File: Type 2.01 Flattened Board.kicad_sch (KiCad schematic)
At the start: 8 parts, among them U10 74AHC125

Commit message: Do the majority of the routing
Drop the i960 header breakout, also don't connect LOCK to the management
engine. I have no idea what it would be useful for. The chipset is the
only thing that will directly interact with the i960 so locking isn't
necessary.
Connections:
- net BUS.PB18: now also U10.10
- net BUS.PB2: now also U10.4
- net BUS.PB4: now also XA2.A3
- net BUS.PB5: now also XA2.A4
- net BUS.PB6: now also XA2.A5
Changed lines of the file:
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@@
-    (stroke (width 0) (type default) (color 0 0 0 0))
-  )
-  (bus_entry (at 246.38 86.36) (size 2.54 2.54)
     (stroke (width 0) (type default) (color 0 0 0 0))
   )
@@
     (stroke (width 0) (type default) (color 0 0 0 0))
   )
-  (bus_entry (at 236.22 86.36) (size 2.54 2.54)
+  (bus_entry (at 241.3 86.36) (size 2.54 2.54)
     (stroke (width 0) (type default) (color 0 0 0 0))
   )
@@
     (stroke (width 0) (type default) (color 0 0 0 0))
   )
-  (bus_entry (at 241.3 86.36) (size 2.54 2.54)
-    (stroke (width 0) (type default) (color 0 0 0 0))
-  )
-  (bus_entry (at 243.84 86.36) (size 2.54 2.54)
-    (stroke (width 0) (type default) (color 0 0 0 0))
-  )
   (bus_entry (at 309.499 142.24) (size 2.54 2.54)
     (stroke (width 0) (type default) (color 0 0 0 0))
@@
     (stroke (width 0) (type default) (color 0 0 0 0))
   )
-  (bus_entry (at 233.68 86.36) (size 2.54 2.54)
-    (stroke (width 0) (type default) (color 0 0 0 0))
-  )
   (bus_entry (at 187.452 106.172) (size 2.54 2.54)
     (stroke (width 0) (type default) (color 0 0 0 0))
@@
     (stroke (width 0) (type default) (color 0 0 0 0))
   )
-  (wire (pts (xy 236.22 88.9) (xy 236.22 102.87))
-    (stroke (width 0) (type default) (color 0 0 0 0))
-  )
   (wire (pts (xy 77.343 253.365) (xy 46.863 253.365))
     (stroke (width 0) (type default) (color 0 0 0 0))
@@
     (stroke (width 0) (type default) (color 0 0 0 0))
   )
-  (wire (pts (xy 238.76 88.9) (xy 238.76 102.87))
-    (stroke (width 0) (type default) (color 0 0 0 0))
-  )
   (wire (pts (xy 139.7 172.212) (xy 187.452 172.212))
     (stroke (width 0) (type default) (color 0 0 0 0))
@@
   )
   (bus (pts (xy 309.499 106.68) (xy 309.499 109.22))
-    (stroke (width 0) (type default) (color 0 0 0 0))
-  )
-  (wire (pts (xy 248.92 88.9) (xy 248.92 102.87))
-    (stroke (width 0) (type default) (color 0 0 0 0))
-  )
-  (wire (pts (xy 246.38 88.9) (xy 246.38 102.87))
     (stroke (width 0) (type default) (color 0 0 0 0))
   )
@@
     (effects (font (size 1.27 1.27)) (justify left bottom))
   )
-  (label "BUS.PB4" (at 28.575 203.2 180)
-    (effects (font (size 1.27 1.27)) (justify right bottom))
+  (label "BUS.PB4" (at 33.655 235.585 0)
+    (effects (font (size 1.27 1.27)) (justify left bottom))
   )
   (label "BUS.PC15" (at 145.288 154.432 0)
@@
     (effects (font (size 1.27 1.27)) (justify right bottom))
   )
+  (label "BUS.PB18" (at 289.56 248.285 180)
+    (effects (font (size 1.27 1.27)) (justify right bottom))
+  )
   (label "BUS.PB12" (at 59.182 80.772 0)
     (effects (font (size 1.27 1.27)) (justify left bottom))
   )
-  (label "BUS.PB1" (at 348.615 95.25 180)
+  (label "BUS.PB1" (at 241.3 89.535 270)
     (effects (font (size 1.27 1.27)) (justify right bottom))
   )
@@
     (effects (font (size 1.27 1.27)) (justify left bottom))
   )
-  (label "BUS.PB6" (at 384.81 86.36 180)
-    (effects (font (size 1.27 1.27)) (justify right bottom))
+  (label "BUS.PB6" (at 33.655 230.505 0)
+    (effects (font (size 1.27 1.27)) (justify left bottom))
   )
   (label "SPI_MOSI" (at 102.87 42.164 270)
@@
     (effects (font (size 1.27 1.27)) (justify left bottom))
   )
-  (label "BUS.PB7" (at 383.54 67.945 180)
+  (label "BUS.PB7" (at 243.84 89.535 270)
     (effects (font (size 1.27 1.27)) (justify right bottom))
   )
@@
     (effects (font (size 1.27 1.27)) (justify right bottom))
   )
-  (label "BUS.PB5" (at 28.575 205.74 180)
-    (effects (font (size 1.27 1.27)) (justify right bottom))
+  (label "BUS.PB5" (at 33.655 233.045 0)
+    (effects (font (size 1.27 1.27)) (justify left bottom))
   )
   (label "GCM4.D7" (at 312.547 124.46 0)
@@
   (label "BUS.PA15" (at 145.288 106.172 0)
     (effects (font (size 1.27 1.27)) (justify left bottom))
+  )
+  (label "BUS.PB2" (at 289.56 228.6 180)
+    (effects (font (size 1.27 1.27)) (justify right bottom))
   )
   (label "BUS.PA17" (at 145.288 139.192 0)
@@
       (reference "C37") (unit 1) (value "0.1uF") (footprint "Capacitor_SMD:C_0805_2012Metric_Pad1.18x1.45mm_HandSolder")
     )
-    (path "/cd4173d7-5549-43d9-b4b1-83989500a84c/15588c18-b55b-4c7c-83c0-ba9a59dc7e6e"
-      (reference "J3") (unit 1) (value "Conn_01x05") (footprint "Connector_PinHeader_2.54mm:PinHeader_1x05_P2.54mm_Vertical")
-    )
     (path "/cd4173d7-5549-43d9-b4b1-83989500a84c/32cf6c22-092f-47a1-90de-a0ed44f63e14"
       (reference "J5") (unit 1) (value "Conn_02x03_Odd_Even") (footprint "Connector_IDC:IDC-Header_2x03_P2.54mm_Horizontal")
@@
       (reference "R3") (unit 1) (value "10k") (footprint "Resistor_SMD:R_0805_2012Metric_Pad1.20x1.40mm_HandSolder")
     )
-    (path "/cd4173d7-5549-43d9-b4b1-83989500a84c/d8f2a0bf-f685-461e-9c59-599184f44107"
-      (reference "R5") (unit 1) (value "10k") (footprint "Resistor_SMD:R_0805_2012Metric_Pad1.20x1.40mm_HandSolder")
-    )
     (path "/cd4173d7-5549-43d9-b4b1-83989500a84c/300496ea-2d26-4906-8c04-178876ec4114"

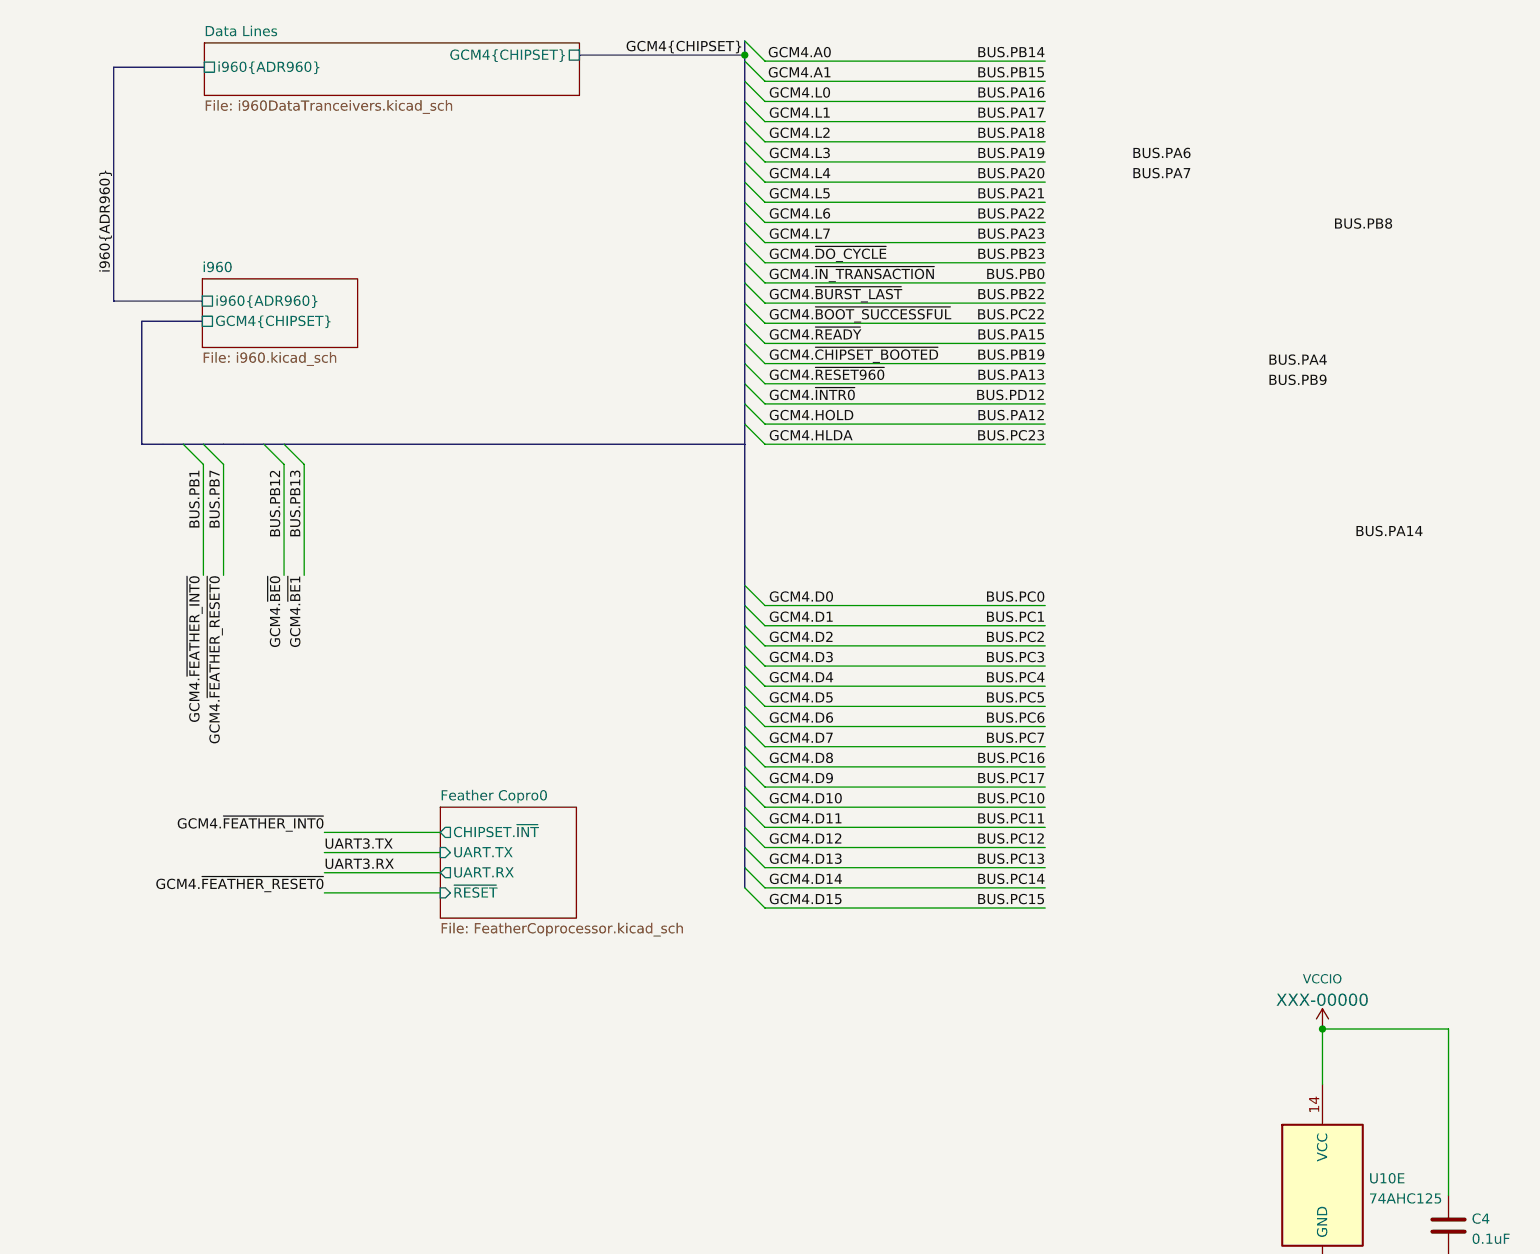
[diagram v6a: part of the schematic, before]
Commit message: Have enough free pins with a serial connection for a second feather coprocessor socket
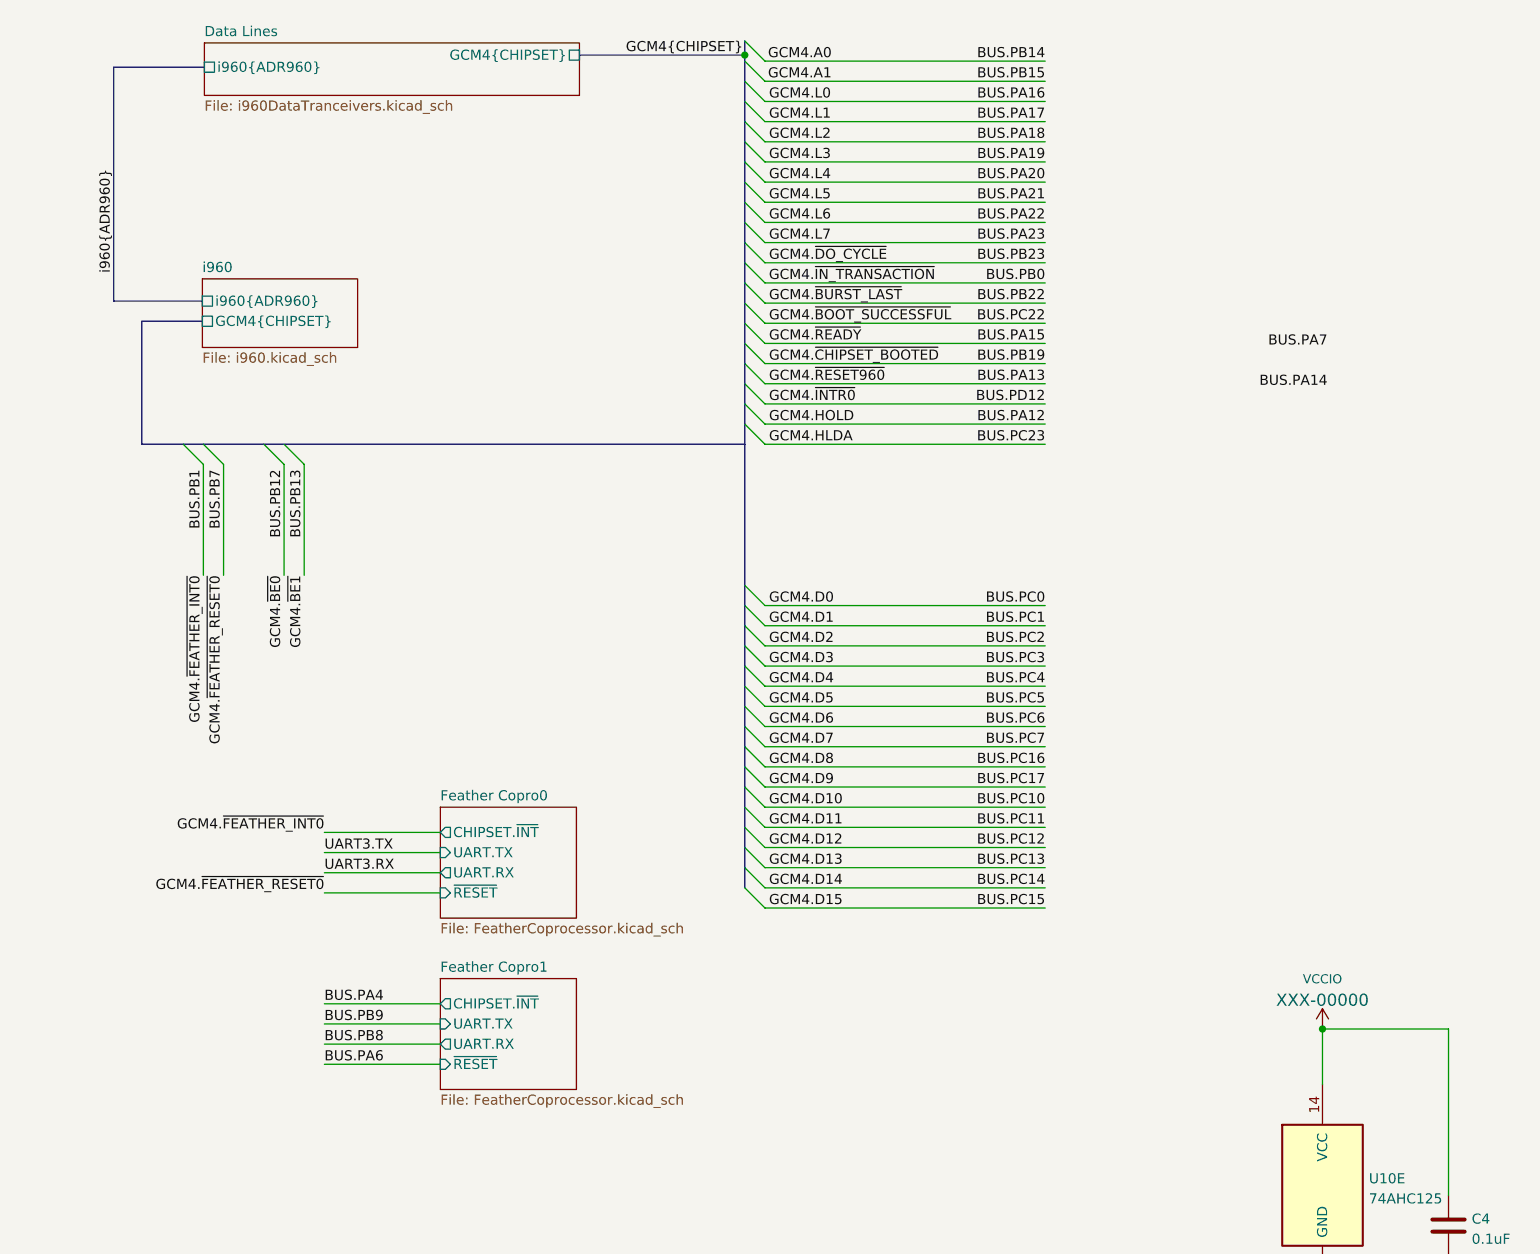
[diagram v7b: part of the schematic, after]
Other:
- added sheet Feather Copro1 (FeatherCoprocessor.kicad_sch)
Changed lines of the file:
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@@
+    (stroke (width 0) (type default) (color 0 0 0 0))
+  )
+  (wire (pts (xy 256.54 164.465) (xy 271.145 164.465))
     (stroke (width 0) (type default) (color 0 0 0 0))
   )
@@
     (stroke (width 0) (type default) (color 0 0 0 0))
   )
+  (wire (pts (xy 256.54 156.845) (xy 271.145 156.845))
+    (stroke (width 0) (type default) (color 0 0 0 0))
+  )
   (bus (pts (xy 309.499 139.7) (xy 309.499 142.24))
     (stroke (width 0) (type default) (color 0 0 0 0))
@@
     (stroke (width 0) (type default) (color 0 0 0 0))
   )
-  (bus (pts (xy 246.38 86.36) (xy 248.92 86.36))
+  (bus (pts (xy 241.3 86.36) (xy 248.92 86.36))
     (stroke (width 0) (type default) (color 0 0 0 0))
   )
@@
     (stroke (width 0) (type default) (color 0 0 0 0))
   )
+  (wire (pts (xy 256.54 159.385) (xy 271.145 159.385))
+    (stroke (width 0) (type default) (color 0 0 0 0))
+  )
   (wire (pts (xy 312.039 116.84) (xy 347.345 116.84))
     (stroke (width 0) (type default) (color 0 0 0 0))
@@
     (stroke (width 0) (type default) (color 0 0 0 0))
   )
-  (bus (pts (xy 233.68 86.36) (xy 236.22 86.36))
+  (bus (pts (xy 233.68 86.36) (xy 238.76 86.36))
     (stroke (width 0) (type default) (color 0 0 0 0))
   )
@@
     (stroke (width 0) (type default) (color 0 0 0 0))
   )
-  (bus (pts (xy 241.3 86.36) (xy 243.84 86.36))
-    (stroke (width 0) (type default) (color 0 0 0 0))
-  )
   (wire (pts (xy 25.908 73.152) (xy 73.66 73.152))
     (stroke (width 0) (type default) (color 0 0 0 0))
@@
     (stroke (width 0) (type default) (color 0 0 0 0))
   )
-  (bus (pts (xy 236.22 86.36) (xy 238.76 86.36))
-    (stroke (width 0) (type default) (color 0 0 0 0))
-  )
   (bus (pts (xy 309.499 106.68) (xy 309.499 109.22))
     (stroke (width 0) (type default) (color 0 0 0 0))
@@
     (stroke (width 0) (type default) (color 0 0 0 0))
   )
+  (wire (pts (xy 256.54 161.925) (xy 271.145 161.925))
+    (stroke (width 0) (type default) (color 0 0 0 0))
+  )
   (bus (pts (xy 23.368 118.872) (xy 23.368 116.332))
     (stroke (width 0) (type default) (color 0 0 0 0))
@@
   )
   (wire (pts (xy 139.7 96.012) (xy 187.452 96.012))
-    (stroke (width 0) (type default) (color 0 0 0 0))
-  )
-  (bus (pts (xy 243.84 86.36) (xy 246.38 86.36))
     (stroke (width 0) (type default) (color 0 0 0 0))
   )
@@
     (effects (font (size 1.27 1.27)) (justify left bottom))
   )
-  (label "BUS.PB8" (at 391.16 59.69 180)
-    (effects (font (size 1.27 1.27)) (justify right bottom))
+  (label "BUS.PB8" (at 256.54 161.925 0)
+    (effects (font (size 1.27 1.27)) (justify left bottom))
   )
   (label "BUS.PB6" (at 61.214 129.032 0)
@@
     (effects (font (size 1.27 1.27)) (justify left bottom))
   )
-  (label "BUS.PA4" (at 382.905 76.835 180)
-    (effects (font (size 1.27 1.27)) (justify right bottom))
+  (label "BUS.PA4" (at 256.54 156.845 0)
+    (effects (font (size 1.27 1.27)) (justify left bottom))
   )
   (label "BUS.PD12" (at 145.288 103.632 0)
@@
     (effects (font (size 1.27 1.27)) (justify left bottom))
   )
-  (label "BUS.PA14" (at 394.97 98.425 180)
+  (label "BUS.PA14" (at 382.905 79.375 180)
     (effects (font (size 1.27 1.27)) (justify right bottom))
   )
@@
     (effects (font (size 1.27 1.27)) (justify right bottom))
   )
-  (label "BUS.PA6" (at 365.76 50.8 180)
-    (effects (font (size 1.27 1.27)) (justify right bottom))
+  (label "BUS.PA6" (at 256.54 164.465 0)
+    (effects (font (size 1.27 1.27)) (justify left bottom))
   )
   (label "BUS.PC1" (at 61.214 116.332 0)
@@
     (effects (font (size 1.27 1.27)) (justify left bottom))
   )
-  (label "BUS.PA7" (at 365.76 53.34 180)
+  (label "BUS.PA7" (at 382.905 74.295 180)
     (effects (font (size 1.27 1.27)) (justify right bottom))
   )
@@
     (effects (font (size 1.27 1.27)) (justify left bottom))
   )
-  (label "BUS.PB9" (at 382.905 79.375 180)
-    (effects (font (size 1.27 1.27)) (justify right bottom))
+  (label "BUS.PB9" (at 256.54 159.385 0)
+    (effects (font (size 1.27 1.27)) (justify left bottom))
   )
   (label "BUS.PB14" (at 347.345 38.1 180)
@@
     (pin "7")
   )
+  (sheet (at 271.145 153.67) (size 17.145 13.97) (fields_autoplaced)
+    (stroke (width 0.1524) (type solid) (color 0 0 0 0))
+    (fill (color 0 0 0 0.0000))
+    (property "Sheet name" "Feather Copro1" (id 0) (at 271.145 152.9584 0)
+      (effects (font (size 1.27 1.27)) (justify left bottom))
+    )
+    (property "Sheet file" "FeatherCoprocessor.kicad_sch" (id 1) (at 271.145 168.2246 0)
+      (effects (font (size 1.27 1.27)) (justify left top))
+    )
+    (pin "CHIPSET.~{INT}" output (at 271.145 156.845 180)
+      (effects (font (size 1.27 1.27)) (justify left))
+    )
+    (pin "UART.TX" input (at 271.145 159.385 180)
+      (effects (font (size 1.27 1.27)) (justify left))
+    )
+    (pin "UART.RX" output (at 271.145 161.925 180)
+      (effects (font (size 1.27 1.27)) (justify left))
+    )
+    (pin "~{RESET}" input (at 271.145 164.465 180)
+      (effects (font (size 1.27 1.27)) (justify left))
+    )
+  )
   (sheet (at 241.427 35.814) (size 47.244 6.604) (fields_autoplaced)
     (stroke (width 0.1524) (type solid) (color 0 0 0 0))
@@
   (sheet_instances
     (path "/" (page "1"))
+    (path "/33147676-43f8-493a-9a6a-8cf437a2c6b4" (page "2"))
     (path "/cd4173d7-5549-43d9-b4b1-83989500a84c/099401c1-0181-4257-be0f-4c7f9d47aefb" (page "3"))
     (path "/c9365d17-b900-4bd3-b96d-5359e9255bd9" (page "7"))
@@
       (reference "#FLG0102") (unit 1) (value "PWR_FLAG") (footprint "")
     )
+    (path "/33147676-43f8-493a-9a6a-8cf437a2c6b4/b66c4163-6664-4006-bf2a-84dc4b6cdd35"
+      (reference "#PWR01") (unit 1) (value "+3.3V") (footprint "")
+    )
+    (path "/33147676-43f8-493a-9a6a-8cf437a2c6b4/83c89139-f22f-4b4b-90fb-04f1f8e1c43a"
+      (reference "#PWR02") (unit 1) (value "GND") (footprint "")
+    )
+    (path "/33147676-43f8-493a-9a6a-8cf437a2c6b4/e2d4f369-3f54-40ad-84cc-25c4a88f6467"
+      (reference "#PWR03") (unit 1) (value "+3.3V") (footprint "")
+    )
+    (path "/33147676-43f8-493a-9a6a-8cf437a2c6b4/89a81393-6658-4b9a-8c17-43b2e30156cc"
+      (reference "#PWR04") (unit 1) (value "+5V") (footprint "")
+    )
     (path "/1197c050-9089-4a58-bf5e-e4f14b5e3552"
       (reference "#PWR05") (unit 1) (value "+3.3V") (footprint "")
@@
       (reference "R7") (unit 1) (value "10k") (footprint "Resistor_SMD:R_0805_2012Metric_Pad1.20x1.40mm_HandSolder")
     )
+    (path "/33147676-43f8-493a-9a6a-8cf437a2c6b4/bef86fba-2eba-47e6-9eba-21b6a503bcdf"
+      (reference "U1") (unit 1) (value "Adafruit_FeatherWing") (footprint "Module:Adafruit_Feather")
+    )
     (path "/cd4173d7-5549-43d9-b4b1-83989500a84c/099401c1-0181-4257-be0f-4c7f9d47aefb/1dff2270-39ed-40b3-865d-e91fbabd717f"
